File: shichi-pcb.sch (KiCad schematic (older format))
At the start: 29 parts, among them J1 USB_C_Receptacle_HRO_TYPE-C-3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, J2 Conn_01x06_Male, J3 Conn_01x04_Male, SW1 SW_Push, SW2 SW_Push, U1 MCP1700-3302E_SOT23, U2 USBLC6-2SC6, U3 STM32F072CBTx

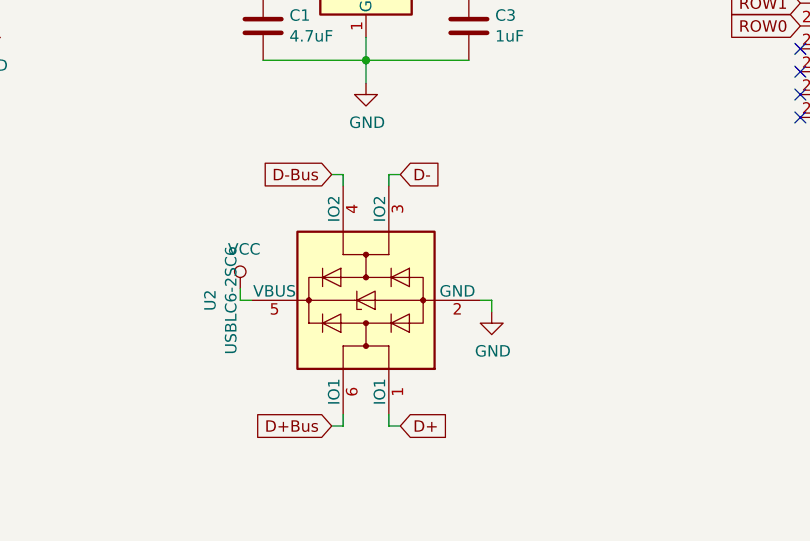
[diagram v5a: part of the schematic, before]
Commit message: Change USBLC6-2SC6 ESD protection device to PRTR5V0U2AX
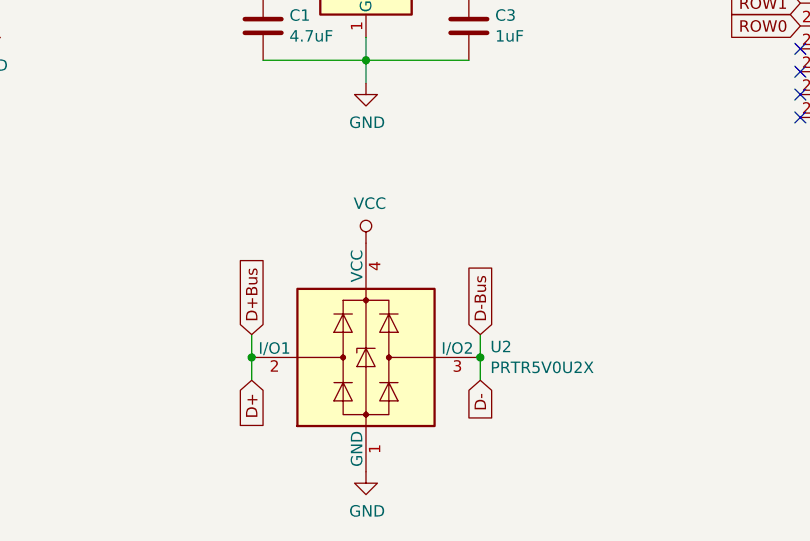
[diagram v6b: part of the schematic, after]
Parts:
- removed U2: USBLC6-2SC6, Package_TO_SOT_SMD:SOT-23-6, symbol Power_Protection:USBLC6-2SC6
- added U2: PRTR5V0U2X, Package_TO_SOT_SMD:SOT-143, symbol Power_Protection:PRTR5V0U2X
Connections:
- net D+Bus is gone; now on net D+: J1.A6 (D+), J1.B6 (D+)
- net D-Bus is gone; now on net D-: J1.A7 (D-), J1.B7 (D-)
- net D+: now also U2.2 (I/O1)
- net D-: now also U2.3 (I/O2)
- net GND: now also U2.1 (GND)
- net VCC: now also U2.4 (VCC)
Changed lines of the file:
@@
 $EndComp
 $Comp
-L power:GND #PWR09
+L power:GND #PWR010
 U 1 1 5CFB408D
 P 4300 3250
-F 0 "#PWR09" H 4300 3000 50  0001 C CNN
+F 0 "#PWR010" H 4300 3000 50  0001 C CNN
 F 1 "GND" H 4305 3077 50  0000 C CNN
 F 2 "" H 4300 3250 50  0001 C CNN
@@
 Wire Wire Line
 	2350 5150 2350 5250
-Wire Wire Line
-	4550 6500 4550 6550
-Wire Wire Line
-	4500 6500 4550 6500
-$Comp
-L power:GND #PWR012
+$Comp
+L power:GND #PWR09
 U 1 1 5D32B978
-P 4550 6550
-F 0 "#PWR012" H 4550 6300 50  0001 C CNN
-F 1 "GND" H 4555 6377 50  0000 C CNN
-F 2 "" H 4550 6550 50  0001 C CNN
-F 3 "" H 4550 6550 50  0001 C CNN
-	1    4550 6550
-	1    0    0    -1
-$EndComp
-Wire Wire Line
-	3450 6450 3450 6500
-Wire Wire Line
-	3450 6500 3500 6500
-$Comp
-L power:VCC #PWR06
+P 4000 7250
+F 0 "#PWR09" H 4000 7000 50  0001 C CNN
+F 1 "GND" H 4005 7077 50  0000 C CNN
+F 2 "" H 4000 7250 50  0001 C CNN
+F 3 "" H 4000 7250 50  0001 C CNN
+	1    4000 7250
+	1    0    0    -1
+$EndComp
+$Comp
+L power:VCC #PWR08
 U 1 1 5D31D96D
-P 3450 6450
-F 0 "#PWR06" H 3450 6300 50  0001 C CNN
-F 1 "VCC" H 3467 6623 50  0000 C CNN
-F 2 "" H 3450 6450 50  0001 C CNN
-F 3 "" H 3450 6450 50  0001 C CNN
-	1    3450 6450
-	1    0    0    -1
-$EndComp
-Wire Wire Line
-	4100 7050 4100 7000
-Wire Wire Line
-	4150 7050 4100 7050
-Text GLabel 4150 7050 2    50   Input ~ 0
+P 4000 6250
+F 0 "#PWR08" H 4000 6100 50  0001 C CNN
+F 1 "VCC" H 4017 6423 50  0000 C CNN
+F 2 "" H 4000 6250 50  0001 C CNN
+F 3 "" H 4000 6250 50  0001 C CNN
+	1    4000 6250
+	1    0    0    -1
+$EndComp
+Text GLabel 3500 6850 3    50   Input ~ 0
 D+
-Wire Wire Line
-	4100 5950 4100 6000
-Wire Wire Line
-	4150 5950 4100 5950
-Text GLabel 4150 5950 2    50   Input ~ 0
+Text GLabel 4500 6850 3    50   Input ~ 0
 D-
-Wire Wire Line
-	3900 7050 3900 7000
-Wire Wire Line
-	3850 7050 3900 7050
-Wire Wire Line
-	3900 5950 3900 6000
-Wire Wire Line
-	3850 5950 3900 5950
-Text GLabel 3850 7050 0    50   Input ~ 0
+Text GLabel 3500 6650 1    50   Input ~ 0
 D+Bus
-Text GLabel 3850 5950 0    50   Input ~ 0
+Text GLabel 4500 6650 1    50   Input ~ 0
 D-Bus
-$Comp
-L Power_Protection:USBLC6-2SC6 U2
-U 1 1 5CF98D69
-P 4000 6500
-F 0 "U2" H 4000 7181 50  0000 C CNN
-F 1 "USBLC6-2SC6" H 4000 7090 50  0000 C CNN
-F 2 "Package_TO_SOT_SMD:SOT-23-6" H 3250 6900 50  0001 C CNN
-F 3 "http://www2.st.com/resource/en/datasheet/CD00050750.pdf" H 4200 6850 50  0001 C CNN
-	1    4000 6500
-	0    -1   -1   0
-$EndComp
 $Comp
 L MCU_ST_STM32F0:STM32F072CBTx U3
@@
 	4450 5050 4450 5150
 $Comp
-L power:+3.3V #PWR011
+L power:+3.3V #PWR012
 U 1 1 5D1ECA69
 P 4450 4950
-F 0 "#PWR011" H 4450 4800 50  0001 C CNN
+F 0 "#PWR012" H 4450 4800 50  0001 C CNN
 F 1 "+3.3V" H 4465 5123 50  0000 C CNN
 F 2 "" H 4450 4950 50  0001 C CNN
@@
 Connection ~ 4450 5050
 $Comp
-L power:GND #PWR08
+L power:GND #PWR07
 U 1 1 5D1FE5B6
 P 4000 5550
-F 0 "#PWR08" H 4000 5300 50  0001 C CNN
+F 0 "#PWR07" H 4000 5300 50  0001 C CNN
 F 1 "GND" H 4005 5377 50  0000 C CNN
 F 2 "" H 4000 5550 50  0001 C CNN
@@
 $EndComp
 $Comp
-L power:+3.3V #PWR010
+L power:+3.3V #PWR011
 U 1 1 5D281CFA
 P 4300 3900
-F 0 "#PWR010" H 4300 3750 50  0001 C CNN
+F 0 "#PWR011" H 4300 3750 50  0001 C CNN
 F 1 "+3.3V" H 4315 4073 50  0000 C CNN
 F 2 "" H 4300 3900 50  0001 C CNN
@@
 $EndComp
 $Comp
-L power:+5V #PWR07
+L power:+5V #PWR06
 U 1 1 5D30778B
 P 3550 4950
-F 0 "#PWR07" H 3550 4800 50  0001 C CNN
+F 0 "#PWR06" H 3550 4800 50  0001 C CNN
 F 1 "+5V" H 3565 5123 50  0000 C CNN
 F 2 "" H 3550 4950 50  0001 C CNN
@@
 NoConn ~ 7200 4600
 NoConn ~ 7200 4700
+$Comp
+L Power_Protection:PRTR5V0U2X U2
+U 1 1 5DB1AA0C
+P 4000 6750
+F 0 "U2" H 4544 6796 50  0000 L CNN
+F 1 "PRTR5V0U2X" H 4544 6705 50  0000 L CNN
+F 2 "Package_TO_SOT_SMD:SOT-143" H 4060 6750 50  0001 C CNN
+F 3 "https://assets.nexperia.com/documents/data-sheet/PRTR5V0U2X.pdf" H 4060 6750 50  0001 C CNN
+	1    4000 6750
+	1    0    0    -1
+$EndComp
+Wire Wire Line
+	4500 6850 4500 6750
+Wire Wire Line
+	3500 6850 3500 6750
+Wire Wire Line
+	3500 6650 3500 6750
+Connection ~ 3500 6750
+Wire Wire Line
+	4500 6650 4500 6750
+Connection ~ 4500 6750
 $EndSCHEMATC

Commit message: Optimize matrix pinout
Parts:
- removed J2: Conn_01x06_Male, Connector_PinSocket_2.54mm:PinSocket_1x06_P2.54mm_Vertical, symbol Connector:Conn_01x06_Male
- added SWD1: Conn_01x05_Male, Miscellaneous_Keyboard_Parts:SWD_Header_1x05_P2.54mm_Vertical, symbol Connector:Conn_01x05_Male
- C3: value 1uF -> 4.7uF
- I2C1: renamed from J3; footprint Connector_PinSocket_2.54mm:PinSocket_1x04_P2.54mm_Vertical -> Miscellaneous_Keyboard_Parts:I2C_Header_1x04_P2.54mm_Vertical
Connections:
- net +3V3: now also I2C1.3 (Pin_3), SWD1.1 (Pin_1)
- net +5V: no longer I2C1.3 (Pin_3)
- net COL0: now also U3.30 (PA9); no longer U3.19 (PB1)
- net COL1: now also U3.29 (PA8); no longer U3.18 (PB0)
- net COL10: now also U3.18 (PB0); no longer U3.41 (PB5)
- net COL11: now also U3.14 (PA4); no longer U3.40 (PB4)
- net COL12: now also U3.11 (PA1); no longer U3.39 (PB3)
- net COL13: now also U3.10 (PA0); no longer U3.38 (PA15)
- net COL2: now also U3.28 (PB15); no longer U3.17 (PA7)
- net COL3: now also U3.27 (PB14); no longer U3.13 (PA3)
- net COL4: now also U3.26 (PB13); no longer U3.12 (PA2)
- net COL5: now also U3.25 (PB12); no longer U3.11 (PA1)
- net COL6: now also U3.22 (PB11); no longer U3.10 (PA0)
- net COL7: now also U3.21 (PB10); no longer U3.2 (PC13)
- net COL8: now also U3.20 (PB2); no longer U3.46 (PB9)
- net COL9: now also U3.19 (PB1); no longer U3.45 (PB8)
- net GND: now also SWD1.3 (Pin_3)
- net NRST: now also SWD1.5 (Pin_5)
- net ROW0: now also U3.17 (PA7); no longer U3.22 (PB11)
- net ROW1: now also U3.16 (PA6); no longer U3.21 (PB10)
- net ROW2: now also U3.15 (PA5); no longer U3.20 (PB2)
- net ROW3: now also U3.13 (PA3); no longer U3.3 (PC14)
- net ROW4: now also U3.12 (PA2); no longer U3.4 (PC15)
- net SWCLK: now also SWD1.2 (Pin_2)
- net SWDIO: now also SWD1.4 (Pin_4)
